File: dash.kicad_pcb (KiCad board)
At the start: 2 copper layers, 48 x 70 mm, 24 parts, among them IC1 ATMEGA328-P, P1 JTAG, P2 ICSP, P3 ESP8266, P4 IN, P5 OUT, U1 LM317T, U2 TLC5916, Y1 16MHz

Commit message: More routing.
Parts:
- moved C4 1.50 mm to (128.0, 135.5), turned to 180 degrees
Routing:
- net Net-(AFF1-Pad1): track 36.4 -> 110.9 mm, vias 0 -> 2
- net Net-(AFF1-Pad5): track 36.9 -> 99.3 mm
- net VCC: track 41.5 -> 84.5 mm, vias 0 -> 2
- net Net-(P5-Pad5): track 0.00 -> 40.0 mm, vias 0 -> 2
- net Net-(IC1-Pad19): track 34.0 -> 72.2 mm, vias 0 -> 1
- net Net-(P4-Pad3): track 34.0 -> 67.3 mm, vias 0 -> 1
- net Net-(AFF1-Pad2): track 40.4 -> 37.3 mm

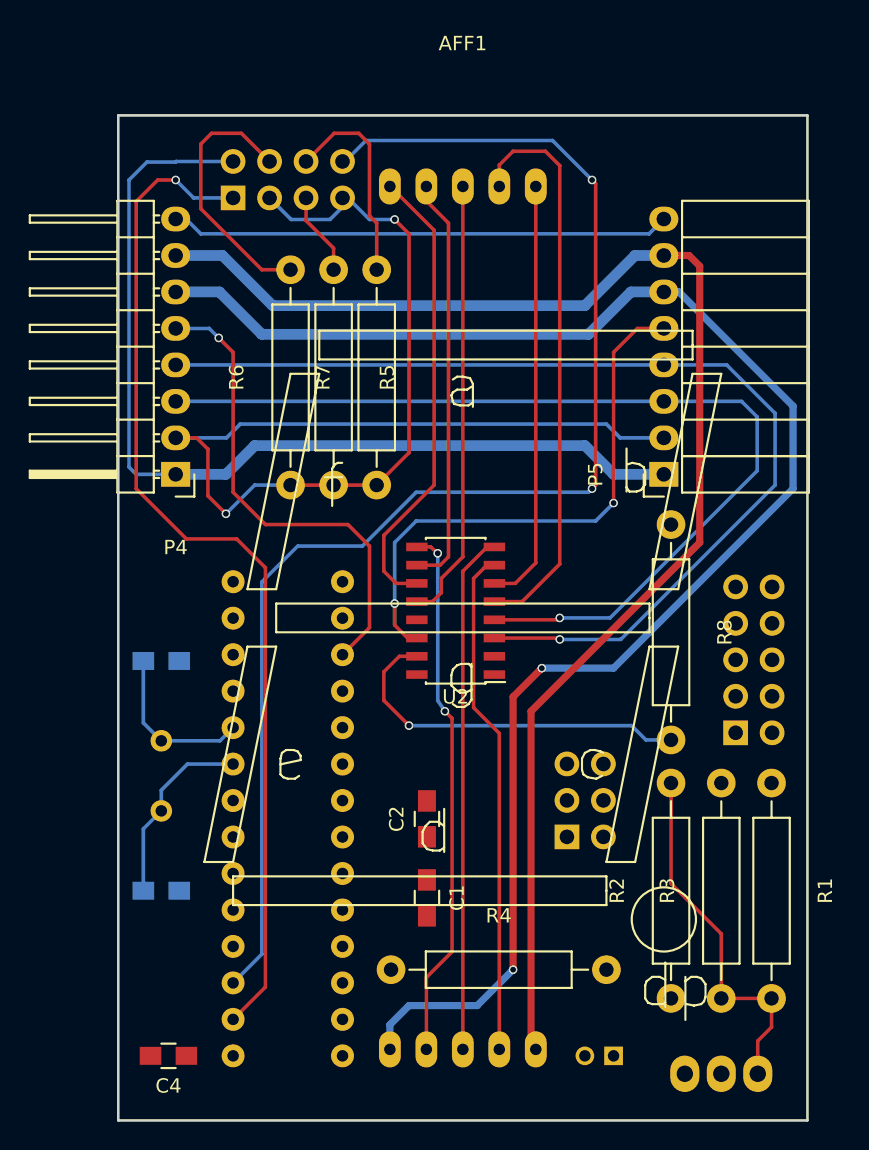
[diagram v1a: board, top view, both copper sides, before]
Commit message: Finished routing. Still missing connection from +12 to red/green anode.
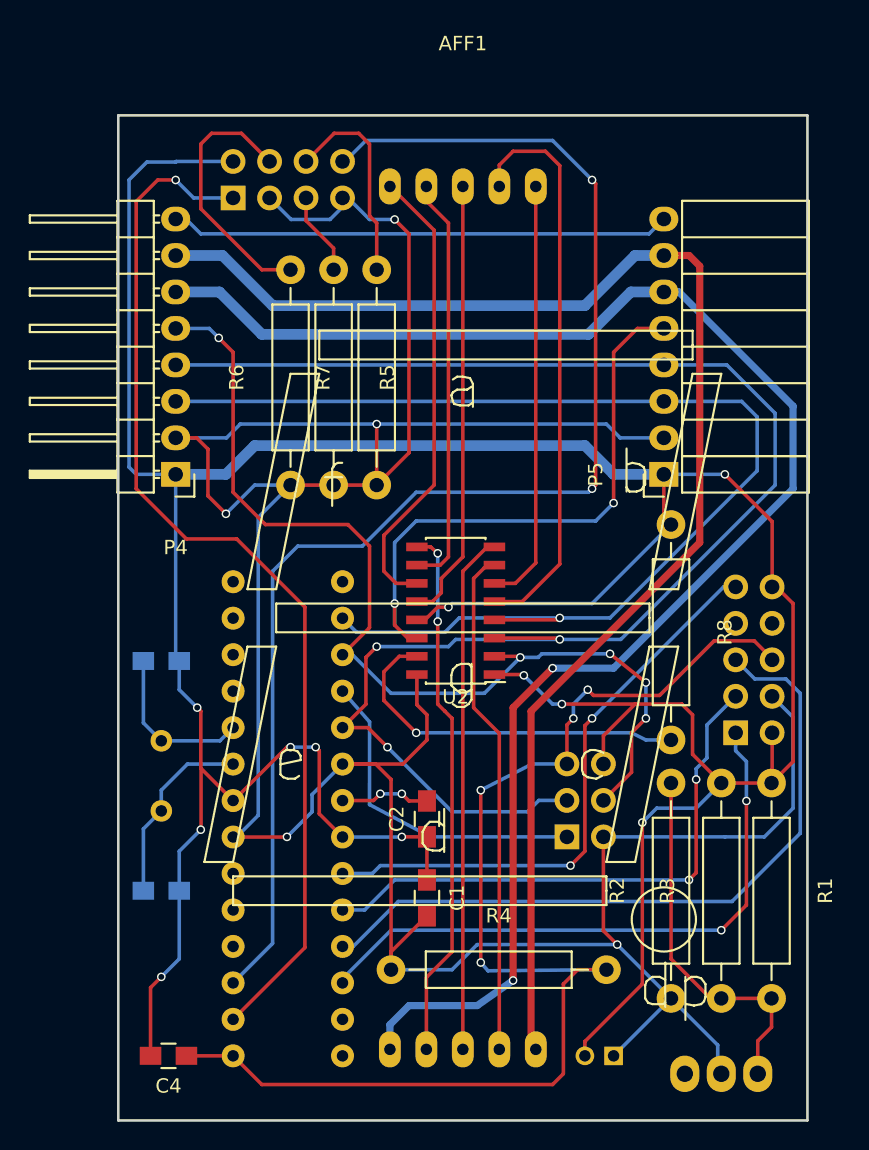
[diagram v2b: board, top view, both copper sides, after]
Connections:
- P4 pad 3: Net-(P4-Pad3) -> Net-(IC1-Pad16)
- P5 pad 3: Net-(P4-Pad3) -> Net-(IC1-Pad16)
- U2 pad 4: Net-(P4-Pad3) -> Net-(IC1-Pad16)
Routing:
- net GND: track 66.9 -> 245.8 mm, vias 0 -> 11
- net VCC: track 84.5 -> 223.2 mm, vias 2 -> 5
- net Net-(C4-Pad1): track 0.00 -> 85.5 mm, vias 0 -> 4
- net Net-(IC1-Pad16): track 0.00 -> 83.2 mm, vias 0 -> 1
- net Net-(P4-Pad3): track 67.3 -> 0.00 mm, vias 1 -> 0
- net Net-(IC1-Pad25): track 0.00 -> 50.4 mm
- net Net-(IC1-Pad26): track 0.00 -> 42.9 mm, vias 0 -> 2
- net Net-(IC1-Pad23): track 0.00 -> 40.8 mm, vias 0 -> 2
- net Net-(IC1-Pad24): track 0.00 -> 39.1 mm, vias 0 -> 2
- net Net-(IC1-Pad19): track 72.2 -> 110.2 mm, vias 1 -> 3
- net Net-(IC1-Pad17): track 33.8 -> 69.2 mm, vias 1 -> 5
- net Net-(IC1-Pad18): track 0.00 -> 23.1 mm
- net Net-(C2-Pad2): track 0.00 -> 6.28 mm, vias 0 -> 2
- net Net-(IC1-Pad2): track 71.6 -> 73.8 mm
